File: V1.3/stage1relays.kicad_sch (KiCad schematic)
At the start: 14 parts, among them T3 AO3400A, T4 AO3400A

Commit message: update v1.3 schematic documentation
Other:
- moved on the sheet: D2, PS1, R26

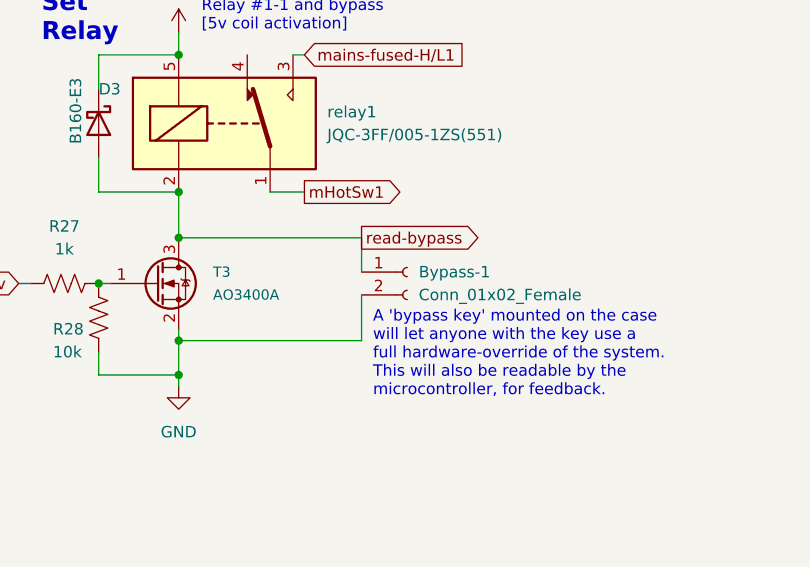
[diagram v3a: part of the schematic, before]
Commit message: started adding the feather footprint to the board. need to update board shape and silkscreens
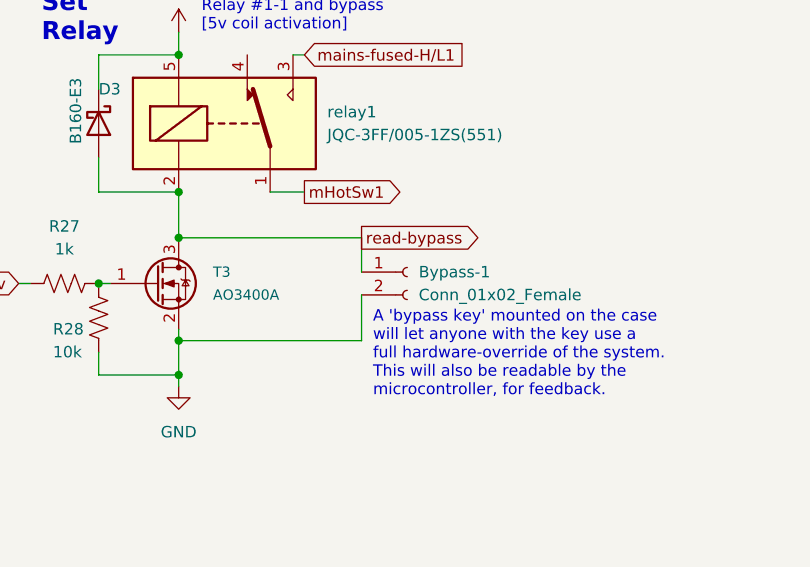
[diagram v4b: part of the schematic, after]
